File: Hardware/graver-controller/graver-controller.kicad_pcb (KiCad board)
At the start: 2 copper layers, 110 x 70 mm, 117 parts, among them J101 DC jack 5.5x2.1, J201 Handpiece, J301 USB-C, J302 SWD, J401 LCD XH 1x7, J402 NMJ6HCD2, Q101 DMP6023LE, Q201 IRLR3410, Q202 SI2309CDS, Q203 BSS123, SW301 BOOT0, SW302 RESET, SW401 EC11E15244G1, U101 LM5164DDAR, U102 AP2112K-3.3, U201 UCC27517DBVR, U202 TLV9062IDR, U301 STM32F411CEU6, U302 USBLC6-2SC6, U401 PESD5V0S2BT, Y301 25MHz 10pF

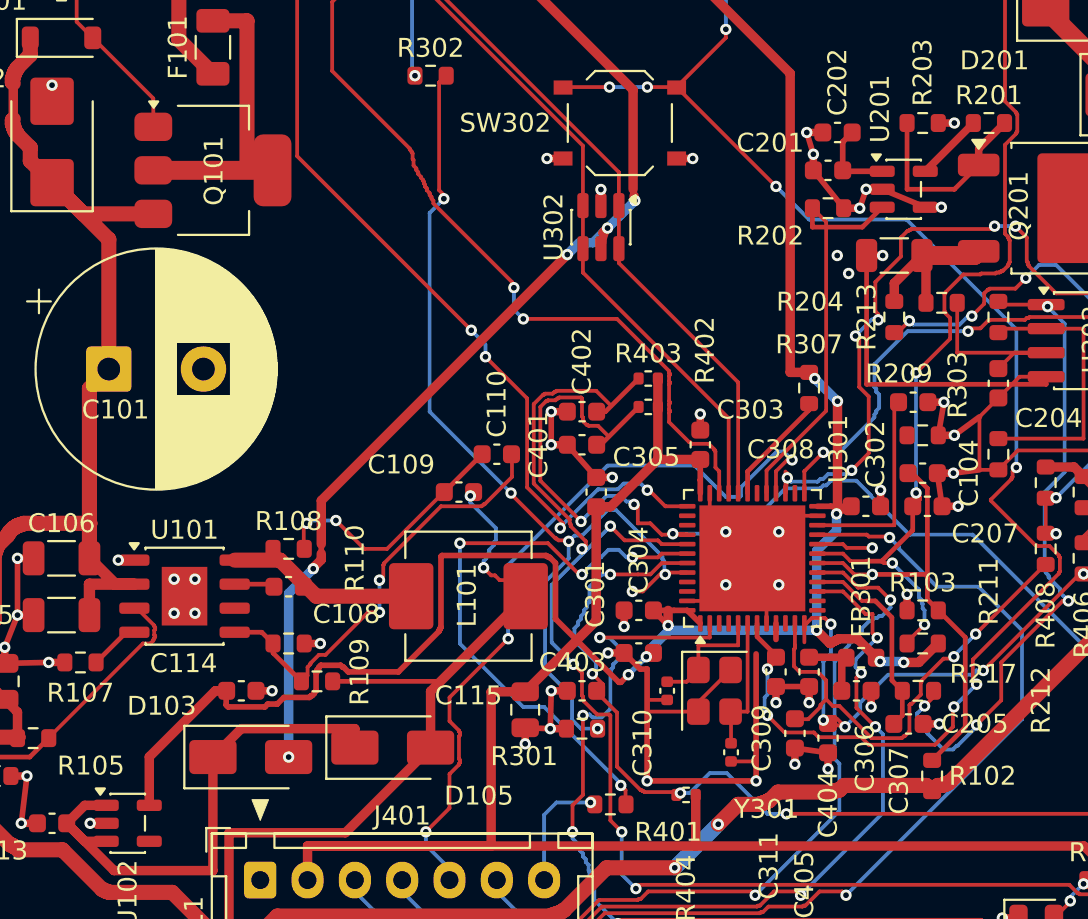
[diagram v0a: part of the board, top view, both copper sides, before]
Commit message: hardware: last three connections drawn by hand, board fully connected
tools/pcb/close_pairs.py draws them into the committed board as the
'manual' group and manual.json keeps them across regeneration:
VDDA pin 9 -> C306 (3.4 mm, 0.30 mm, 2 vias), PB2 via -> R303 (6.3 mm,
0.20 mm, 1 via), +5V U102/D105 -> C201 (63 mm, 0.30 mm, 10 vias) with
one 1.6 mm crossing under the USB pair at 90 degrees on B.Cu, 0.6 mm
from the pair, whitelisted in the USB reference check. To make room:
+3V3's B.Cu trunk doglegged 0.4 mm, PEDAL_RING's dead stub shortened,
ENC_A re-routed on B.Cu (7 -> 18 mm, 2 more vias). manual.py bug fixed
(the manual group was listed as scripted, so export collected nothing).

kicad-cli with the width rules: 0 errors, 0 parity, 0 unconnected,
12 warnings (4 clipped connector silk, 8 dangling fanout stubs on
unused pins). Width floors 8/8, sense ground 5/5, no GND islands,
no ADC net parallel to a switching net.
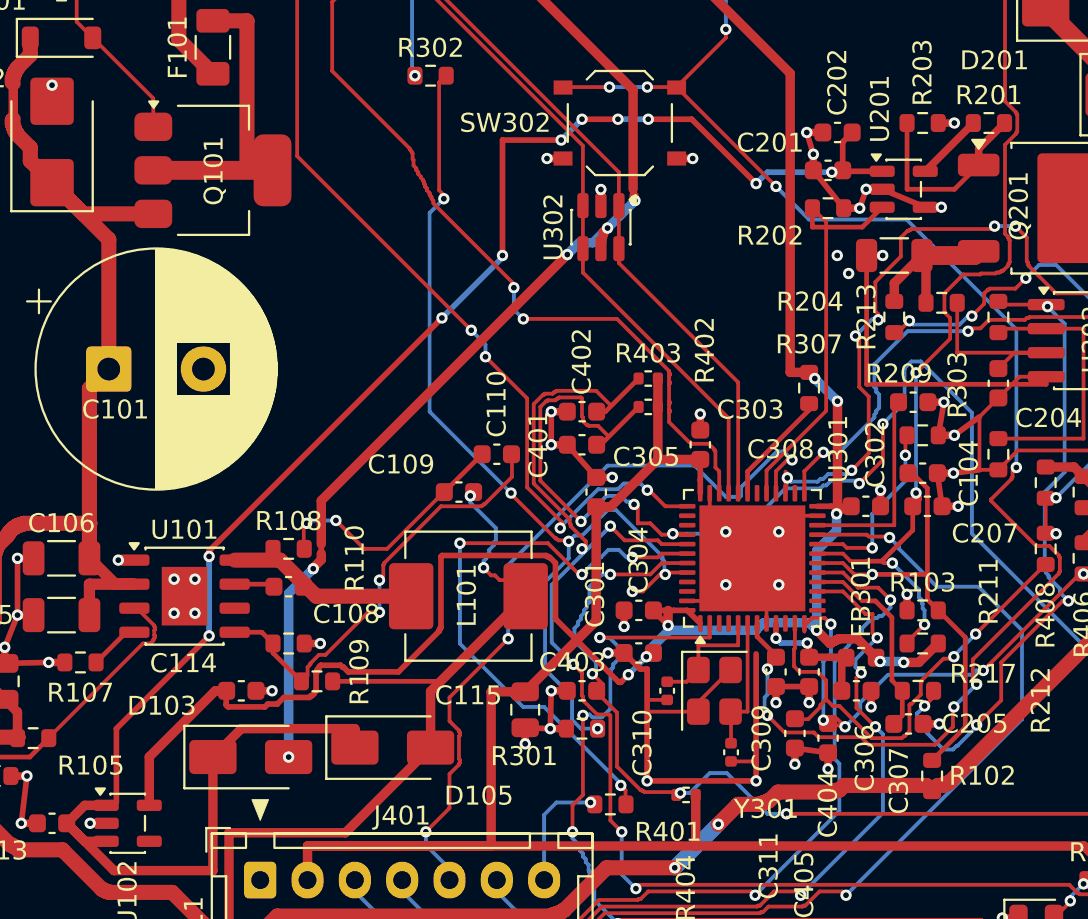
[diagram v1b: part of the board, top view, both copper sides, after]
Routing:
- net +5V: track 33.2 -> 96.4 mm, vias 0 -> 10
- net ENC_A: track 68.7 -> 79.8 mm, vias 4 -> 6
- net Net-(U301-PB2): track 2.98 -> 9.31 mm, vias 1 -> 2
- net /MCU/VDDA: track 4.67 -> 7.22 mm, vias 0 -> 2
- net PEDAL_RING: track 26.3 -> 25.7 mm

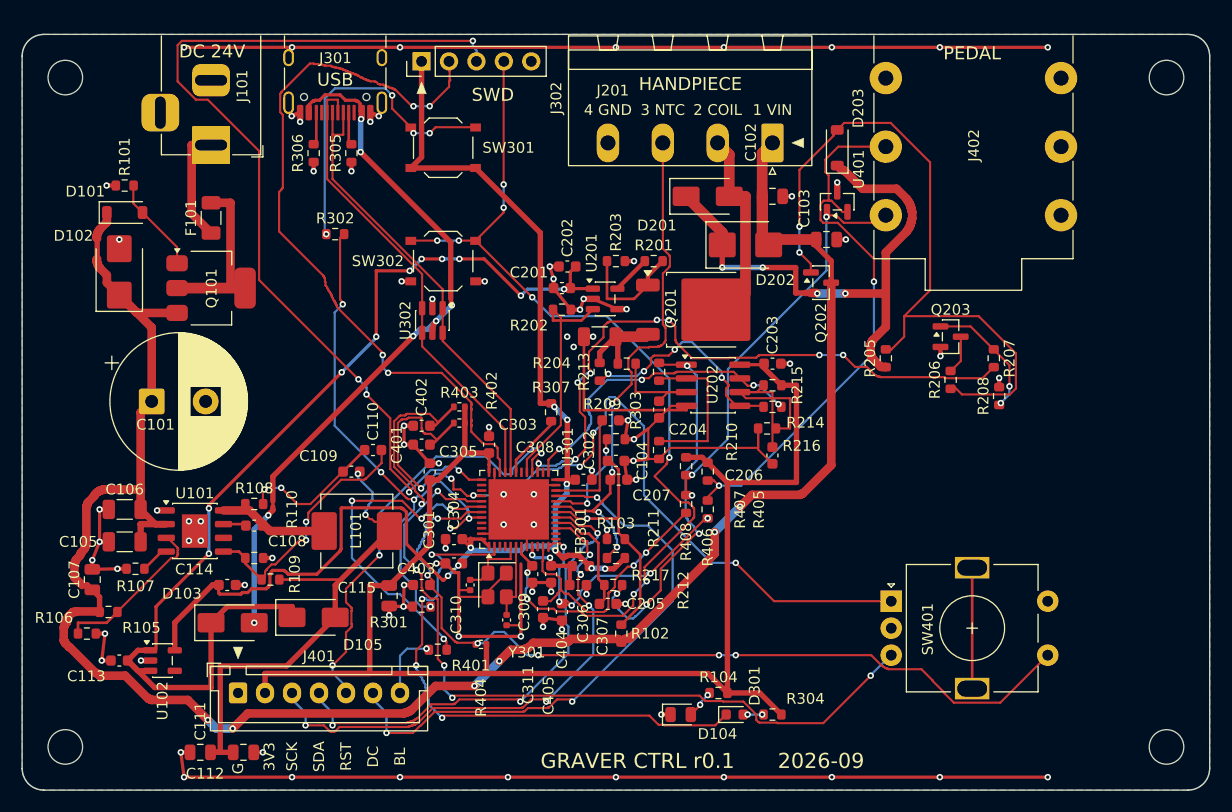
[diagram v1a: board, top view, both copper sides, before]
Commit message: hardware: wire pads instead of connectors, board to 95 x 70
ADR 0003 Decision 9. Every board connector except USB-C becomes a row of
plated through-holes and the rotary encoder moves off the board onto wires;
Jan solders the looms at box build. The mating halves were the sourcing
problem, not the board halves, and the four connectors dropped here were
also the four parts whose footprints were still unverified against real
hardware.

Schematic (ERC 0, netlist diffed pad-by-pad - every difference was an
auto-generated net NAME following its anchor pin, no connectivity changed):

- J101 Barrel_Jack_Switch -> Conn_01x02, SolderWire-1sqmm 1x02, 1.4 mm
- J201 -> PinHeader_1x04, J401 -> PinHeader_1x07
- J402 AudioJack3_SwitchTR -> Conn_01x04 (TIP, RN, RING, SLV)
- SW401 RotaryEncoder_Switch_MP -> J403 Conn_01x04 (A, GND, B, SW)
- the five pad rows carry no LCSC/MPN: they are holes, not parts, and an
  empty field reads as a schematic-parity mismatch
- three orphaned no-connect flags removed with the old unused pins

Board 110 x 70 -> 95 x 70: measured on the routed board, everything except
the connectors, the encoder and the mounting holes fits in 84.5 x 64.0 mm,
so the connectors were setting the width. 95 also brings the long side
under JLC's 100 x 100 price band.

State: 0 DRC errors, 0 schematic parity, 3 unconnected pad pairs (+5V and
two GND, all short same-net gaps), 11 warnings, 126 vias, all placement
checks and ADR criteria PASS, all eight per-net width floors PASS.

Tooling:

- outline 95 x 70 in place.py, copper.py, silk.py and render.sh
- rear pad rows inset from the edge (negative overhang): J101's 2.7 mm pads
  sitting flush broke the 0.3 mm copper-to-edge rule
- silk legends rewritten; the two MIDDLE pads of each 1x4 rear row had no
  sideways escape at 2.54 mm pitch and silently got no label, which on the
  handpiece row is 24 V versus the NTC input. Pin numbers dropped and the
  seed pushed to 3.6 mm; 24 of 24 legends now place on seed.
- copper.py BRIDGE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
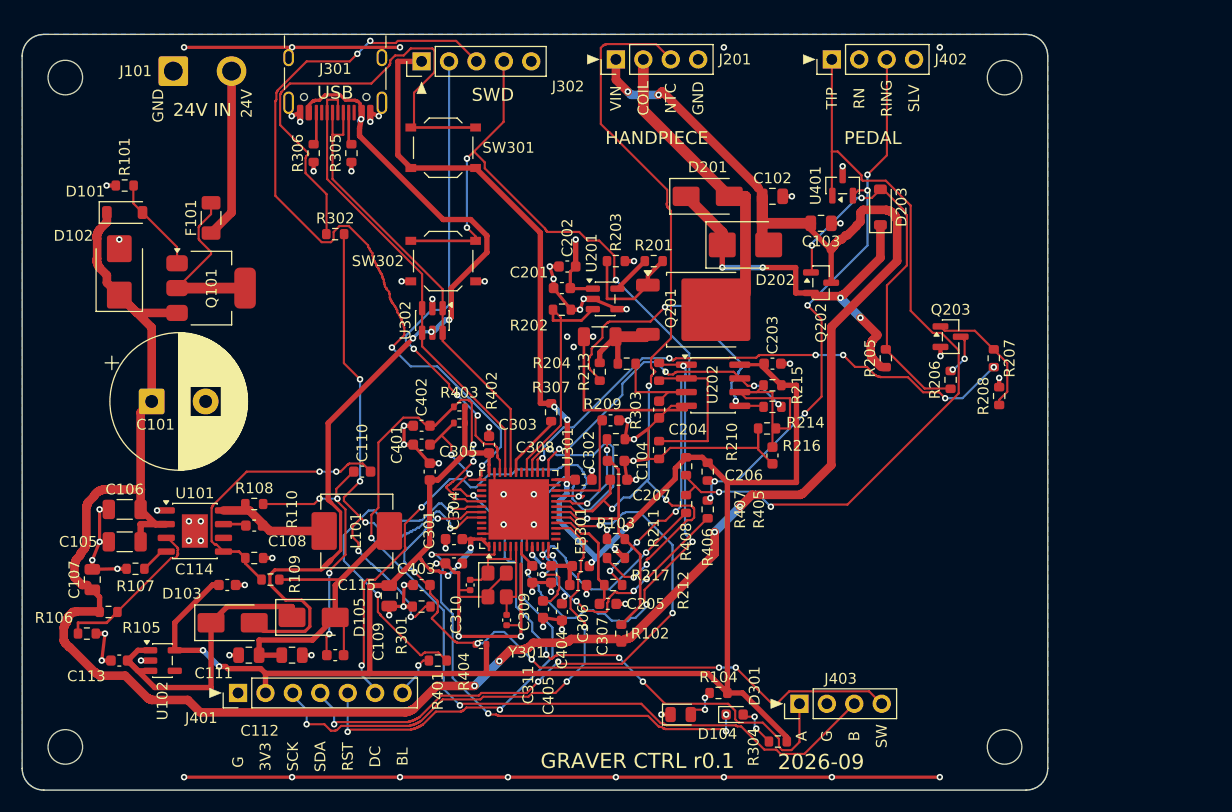
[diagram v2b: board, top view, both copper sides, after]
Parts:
- removed SW401: EC11E15244G1, Rotary_Encoder:RotaryEncoder_Alps_EC11E-Switch_Vertical_H20mm
- added J403: Encoder pads 1x4, Connector_PinHeader_2.54mm:PinHeader_1x04_P2.54mm_Vertical, F.Cu at (122.0, 112.0)
- J101: value DC jack 5.5x2.1 -> Power in 2p; footprint Connector_BarrelJack:BarrelJack_Horizontal -> Connector_Wire:SolderWire-1sqmm_1x02_P5.4mm_D1.4mm_OD2.7mm
- J201: value Handpiece -> Handpiece pads 1x4; footprint Connector_Phoenix_MSTB:PhoenixContact_MSTBA_2,5_4-G-5,08_1x04_P5.08mm_Horizontal -> Connector_PinHeader_2.54mm:PinHeader_1x04_P2.54mm_Vertical
- J401: value LCD XH 1x7 -> LCD pads 1x7; footprint Connector_JST:JST_XH_B7B-XH-A_1x07_P2.50mm_Vertical -> Connector_PinHeader_2.54mm:PinHeader_1x07_P2.54mm_Vertical
- J402: value NMJ6HCD2 -> Pedal pads 1x4; footprint Connector_Audio:Jack_6.35mm_Neutrik_NMJ6HCD2_Horizontal -> Connector_PinHeader_2.54mm:PinHeader_1x04_P2.54mm_Vertical
- moved C109 17.1 mm to (79.0, 107.5)
- moved J201 16.4 mm to (105.0, 52.3), turned to 90 degrees
- moved J402 15.3 mm to (125.0, 52.3)
- moved MH402 15.0 mm to (141.0, 54.0)
- moved MH403 15.0 mm to (141.0, 116.0)
- moved C111 10.1 mm to (71.0, 107.5)
- moved C112 10.1 mm to (75.0, 107.5)
- moved J101 7.69 mm to (64.0, 53.4), turned to 0 degrees
- moved D203 6.80 mm to (129.5, 66.0)
- moved R304 2.55 mm to (120.0, 115.5)
- moved C110 2.24 mm to (81.5, 90.5)
- moved C103 1.58 mm to (124.0, 67.5)
- moved U401 1.58 mm to (126.0, 64.0)
- moved R401 1.00 mm to (88.5, 108.0)
- turned J401 to 90 degrees
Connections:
- F101 pad 1: Net-(F101-Pad1) -> Net-(J101-Pin_2)
- J101 pad 1: Net-(F101-Pad1) -> GND
- J101 pad 2: GND -> Net-(J101-Pin_2)
- R405 pad 2: Net-(U401-A2) -> Net-(J402-Pin_3)
- R406 pad 1: Net-(U401-A2) -> Net-(J402-Pin_3)
- R407 pad 2: Net-(U401-A1) -> Net-(J402-Pin_1)
- R408 pad 1: Net-(U401-A1) -> Net-(J402-Pin_1)
- U401 pad 1: Net-(U401-A1) -> Net-(J402-Pin_1)
- U401 pad 2: Net-(U401-A2) -> Net-(J402-Pin_3)
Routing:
- net Net-(J402-Pin_1): track 0.00 -> 73.3 mm, vias 0 -> 2
- net GND: track 316.7 -> 244.3 mm, vias 87 -> 83
- net +5V: track 96.4 -> 35.7 mm, vias 10 -> 1
- net Net-(U401-A2): track 52.3 -> 0.00 mm, vias 2 -> 0
- net Net-(J402-Pin_3): track 0.00 -> 51.3 mm, vias 0 -> 6
- net Net-(U401-A1): track 37.8 -> 0.00 mm, vias 3 -> 0
- net NTC: track 48.8 -> 81.2 mm, vias 4 -> 5
- net Net-(D203-A): track 66.4 -> 34.4 mm
- net VIN: track 193.9 -> 222.3 mm
- net LCD_RST: track 41.0 -> 65.9 mm
- net SWDIO: track 68.0 -> 44.5 mm, vias 4 -> 3
- net +3V3: track 268.3 -> 249.7 mm, vias 9 -> 11
- net ENC_A: track 79.8 -> 62.4 mm
- net Net-(D105-A): track 53.4 -> 36.3 mm, vias 2 -> 0
- net ENC_SW: track 78.7 -> 62.8 mm
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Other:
- board size 110 x 70 mm -> 95 x 70 mm
- board text added: "24V"
- board text added: "24V IN"
- board text added: "A"
- board text added: "B"
- board text added: "COIL"
- board text added: "GND"
- board text added: "NTC"
- board text added: "RING"
- board text added: "RN"
- board text added: "SLV"
- board text added: "SW"
- board text added: "TIP"
- board text added: "VIN"
- board text removed: "1 VIN"
- board text removed: "2 COIL"
- board text removed: "3 NTC"
- board text removed: "4 GND"
- board text removed: "DC 24V"

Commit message: hardware: board electrically complete, last 3 pairs closed by hand
0 DRC errors, 0 schematic parity, 0 unconnected, 11 warnings. All eight
per-net width floors PASS, GND islands and the sense-ground tree PASS, one
allowed USB crossing and no disallowed ones.

The autorouter left three pairs open: +5V D105.1 -> C201.1 (the ORing
Schottky to the gate driver's supply cap - without it the driver sits in
UVLO and the board never fires) and two short GND stubs. Closed with a new
tools/pcb/close_open.py, then captured into manual.json with
place.py --export-manual: 38 items, 33 on +5V and 5 on GND.

close_open.py is a thin driver over the GOOD half of close_pairs.py - the
two-layer clearance grid, the Dijkstra, the octilinear simplifier, the
manual grouping - with targets found by pad name or by point instead of by
coordinate table. close_pairs.py itself stays stale: its NUDGES, RIPUPS and
VDDA_COMMITTED name tracks that no longer exist.

Three things learned, all now enforced in code or comment:

- The USB pair walls the board in half. With its B.Cu shadow respected there
  is NO +5V path from the power block to the gate driver, and a search
  allowed to ignore the shadow came back crossing the run twice at a shallow
  angle - usb_reference_check refused it, correctly. The answer is the one
  the old board used: a single short perpendicular crossing at a site chosen
  for clearance, 1.56 mm of B.Cu at 90 degrees, 0.60 mm off the nearest pair
  track. USB_CROSSING_OK moves from (36.45, 21.35) to (31.62, 16.77).
- group_manual replaces the whole manual group with whatever the current run
  drew, so a run that skipped a target as "already joined" deleted the copper
  that joined it - two runs ping-pong between the +5V route and the GND
  stubs. Hence strip_manual(): start from the autorouted baseline every run
  and redraw every target. The script owns that group.
- A hand route or bridge on a Power-class net must carry that net's
  .kicad_dru floor, not W_SIG.

The +5V run 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
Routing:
- net +5V: track 35.7 -> 103.9 mm, vias 1 -> 11
- net GND: track 244.3 -> 254.5 mm, vias 83 -> 85
